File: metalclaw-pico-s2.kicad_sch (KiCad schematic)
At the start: 73 parts, among them J1 USB_C_Receptacle_USB2.0_14P, J2 Conn_01x05, J3 Conn_02x05_Odd_Even, J4 Conn_Coaxial, SW1 SW_Push, SW2 SW_Push, U1 ESP32-S2, U2 MX25L3236FM2I-08G-TR, U3 APS6404L-3SQRx-SN, U5 XC6220B331MR, Y1 XRCGB40M000F1S2FR0

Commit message: Assign more part numbers
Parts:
- C10, C11, C2: footprint (none) -> Capacitor_SMD:C_0402_1005Metric
- C12, C13, C16, C17: footprint Capacitor_SMD:C_0402_1005Metric -> Capacitor_SMD:C_0201_0603Metric
- C14, C15, C4, C7, C8, C9: footprint (none) -> Capacitor_SMD:C_0201_0603Metric
- C5, C6: footprint Capacitor_SMD:C_0402_1005Metric -> Capacitor_SMD:C_0201_0603Metric; Mouser GRT1555C1H6R0DA02D -> 81-GRM0335C1E6R0BA1D
- D1: footprint (none) -> Diode_SMD:D_SOD-323F; Mouser (none) -> 757-CUHS20F30H3F
- L1: footprint Inductor_SMD:L_0402_1005Metric -> Inductor_SMD:L_0201_0603Metric
- R1, R17, R29, R30, R31, R32, R33, R34, R35, R36, R37, R38, R39, R40, R41, R42: footprint Resistor_SMD:R_0402_1005Metric -> Resistor_SMD:R_0201_0603Metric; Mouser (none) -> 71-CRCW02015K10FEDAT
- R10, R11, R12, R13, R14, R15, R16, R18, R19, R2, R20, R21, R22, R23, R24, R25, R26, R27, R28, R3, R4, R5, R6, R7, R8, R9: footprint Resistor_SMD:R_0402_1005Metric -> Resistor_SMD:R_0201_0603Metric; Mouser (none) -> 603-AC0201FR-13220RL
- SW1, SW2: footprint Button_Switch_SMD:SW_Push_SPST_NO_Alps_SKRK -> Button_Switch_SMD:SW_SPST_PTS810; Mouser (none) -> 611-PTS810SJM250SMTR

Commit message: Remove unecessary symbol fields
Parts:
- Y1: private KLC_S4.1 -> (none)
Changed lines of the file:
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@@
-			)
-		)
-		(property private "KLC_S3.3" "The rectangle is not a symbol body but a graphical element"
-			(at 135.89 139.7 0)
-			(show_name yes)
-			(effects
-				(font
-					(size 1.27 1.27)
-				)
-				(hide yes)
-			)
-		)
-		(property private "KLC_S4.1" "Some pins are on 50mil grid to make the symbol small"
-			(at 138.43 139.7 0)
-			(show_name yes)
-			(effects
-				(font
-					(size 1.27 1.27)
-				)
-				(hide yes)
 			)
 		)

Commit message: Specify more passive component parts
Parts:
- C1, C3: Mouser 0603X106M100CT -> 791-0603X106M100CT
- C10, C11, C2: Mouser (none) -> 791-0201X105M100CT
- C14, C15, C16, C17, C4, C7, C8, C9: Mouser (none) -> 81-GRM033R61A104ME5D
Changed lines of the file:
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@@
 			)
 		)
+		(property "Mouser" "81-GRM033R61A104ME5D "
+			(at 40.64 125.73 90)
+			(effects
+				(font
+					(size 1.27 1.27)
+				)
+				(hide yes)
+			)
+		)
 		(pin "1"
 		)
@@
 			)
 		)
+		(property "Mouser" "81-GRM033R61A104ME5D "
+			(at 40.64 138.43 90)
+			(effects
+				(font
+					(size 1.27 1.27)
+				)
+				(hide yes)
+			)
+		)
 		(pin "1"
 		)
@@
 			)
 		)
+		(property "Mouser" "81-GRM033R61A104ME5D "
+			(at 40.64 151.13 90)
+			(effects
+				(font
+					(size 1.27 1.27)
+				)
+				(hide yes)
+			)
+		)
 		(pin "1"
 		)
@@
 			)
 		)
+		(property "Mouser" "81-GRM033R61A104ME5D "
+			(at 40.64 144.78 90)
+			(effects
+				(font
+					(size 1.27 1.27)
+				)
+				(hide yes)
+			)
+		)
 		(pin "1"
 		)
@@
 			)
 		)
-		(property "Mouser" "0603X106M100CT"
+		(property "Mouser" "791-0603X106M100CT "
 			(at 220.98 45.72 0)
 			(effects
@@
 			)
 		)
+		(property "Mouser" "81-GRM033R61A104ME5D "
+			(at 40.64 132.08 90)
+			(effects
+				(font
+					(size 1.27 1.27)
+				)
+				(hide yes)
+			)
+		)
 		(pin "1"
 		)
@@
 			)
 		)
+		(property "Mouser" "81-GRM033R61A104ME5D "
+			(at 193.04 52.07 90)
+			(effects
+				(font
+					(size 1.27 1.27)
+				)
+				(hide yes)
+			)
+		)
 		(pin "1"
 		)
@@
 			)
 		)
-		(property "Mouser" "0603X106M100CT"
+		(property "Mouser" "791-0603X106M100CT "
 			(at 266.7 45.72 0)
 			(effects
@@
 			)
 		)
+		(property "Mouser" "791-0201X105M100CT "
+			(at 40.64 163.83 90)
+			(effects
+				(font
+					(size 1.27 1.27)
+				)
+				(hide yes)
+			)
+		)
 		(pin "1"
 		)
@@
 			)
 		)
+		(property "Mouser" "81-GRM033R61A104ME5D "
+			(at 175.26 52.07 90)
+			(effects
+				(font
+					(size 1.27 1.27)
+				)
+				(hide yes)
+			)
+		)
 		(pin "1"
 		)
@@
 			)
 		)
+		(property "Mouser" "791-0201X105M100CT "
+			(at 40.64 170.18 90)
+			(effects
+				(font
+					(size 1.27 1.27)
+				)
+				(hide yes)
+			)
+		)
 		(pin "1"
 		)
@@
 			)
 		)
+		(property "Mouser" "791-0201X105M100CT "
+			(at 115.57 160.02 90)
+			(effects
+				(font
+					(size 1.27 1.27)
+				)
+				(hide yes)
+			)
+		)
 		(pin "2"
 		)
@@
 			(effects
 				(font
+					(size 1.27 1.27)
+				)
+				(hide yes)
+			)
+		)
+		(property "Mouser" "81-GRM033R61A104ME5D "
+			(at 40.64 157.48 90)
+			(effects
+				(font

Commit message: Some refinements to schematic and layout
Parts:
- C12, C13, J4, L1: now not fitted
- C16, C17: value 100n -> 1u; Mouser 81-GRM033R61A104ME5D -> 791-0201X105M100CT
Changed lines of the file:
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@@
 		(in_bom yes)
 		(on_board yes)
-		(dnp no)
+		(dnp yes)
 		(property "Reference" "C13"
 			(at 132.334 75.692 90)
@@
 		(dnp no)
 		(property "Reference" "C17"
-			(at 188.976 50.292 90)
+			(at 186.182 53.086 0)
 			(effects
 				(font
@@
 			)
 		)
-		(property "Value" "100n"
-			(at 186.69 49.784 90)
+		(property "Value" "1u"
+			(at 187.452 50.8 0)
 			(effects
 				(font
@@
 			)
 		)
-		(property "Mouser" "81-GRM033R61A104ME5D "
+		(property "Mouser" "791-0201X105M100CT "
 			(at 193.04 52.07 90)
 			(effects
@@
 		(in_bom yes)
 		(on_board yes)
-		(dnp no)
+		(dnp yes)
 		(property "Reference" "C12"
 			(at 132.334 86.106 90)
@@
 		(in_bom yes)
 		(on_board yes)
-		(dnp no)
+		(dnp yes)
 		(property "Reference" "J4"
 			(at 147.828 72.136 90)
@@
 		(dnp no)
 		(property "Reference" "C16"
-			(at 171.196 50.292 90)
+			(at 168.402 53.086 0)
 			(effects
 				(font
@@
 			)
 		)
-		(property "Value" "100n"
-			(at 168.91 49.784 90)
+		(property "Value" "1u"
+			(at 169.672 50.546 0)
 			(effects
 				(font
@@
 			)
 		)
-		(property "Mouser" "81-GRM033R61A104ME5D "
+		(property "Mouser" "791-0201X105M100CT "
 			(at 175.26 52.07 90)
 			(effects
@@
 		(in_bom yes)
 		(on_board yes)
-		(dnp no)
+		(dnp yes)
 		(property "Reference" "L1"
 			(at 114.808 77.47 0)

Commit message: Fix all ERC errors and warnings
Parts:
- removed D1: D_Schottky, Diode_SMD:D_SOD-323F, symbol Device:D_Schottky
- added JP1: Jumper_2_Bridged, symbol Jumper:Jumper_2_Bridged
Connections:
- net +3V3: no longer A2.36 (3V3), U1.30 (VDD_SPI)
- net GND: now also JP1.2 (B); no longer A2.33 (AGND)
- net GP14: no longer R27.2, R31.2, R40.2, U1.55 (GPIO46)
- net GP6: no longer R17.2, R19.2, U1.21 (XTAL_32K_P)
- net VBUS: now also C1.1, U5.1 (VIN), U5.3 (CE)
- net +3.3V renamed VDD
- net VDD: now also U1.30 (VDD_SPI)
- removed net VS: A2.39 (VSYS), C1.1, U5.1 (VIN), U5.3 (CE)
- new net: A2.33 (AGND), JP1.1 (A)
- new net GP15: R27.2, R31.2, R40.2, U1.55 (GPIO46)
- new net GP7: R17.2, R19.2, U1.21 (XTAL_32K_P)
- no-connect marks 2 -> 4

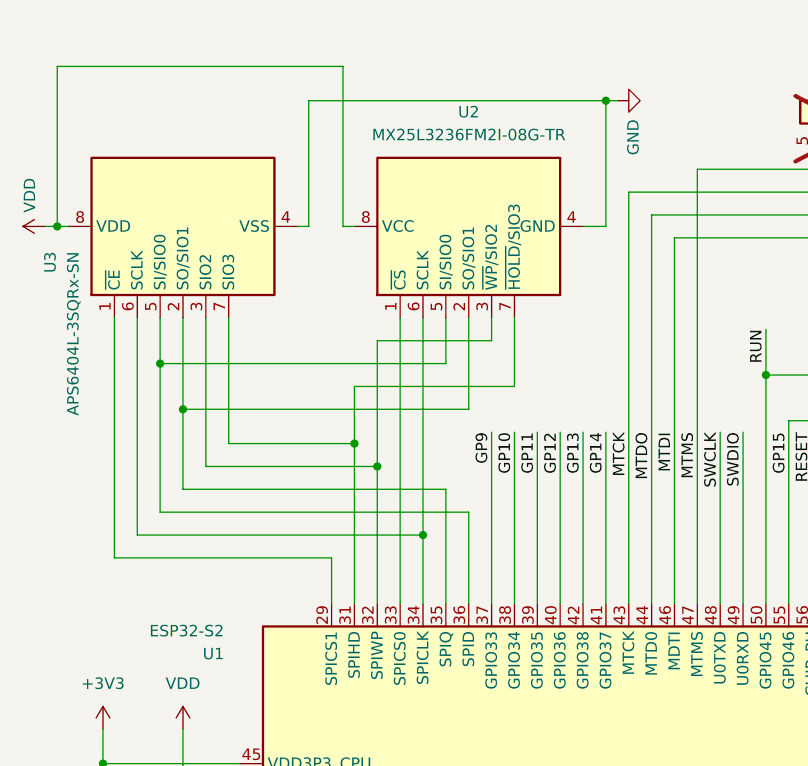
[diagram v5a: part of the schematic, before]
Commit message: Add bypass caps to PSRAM and flash
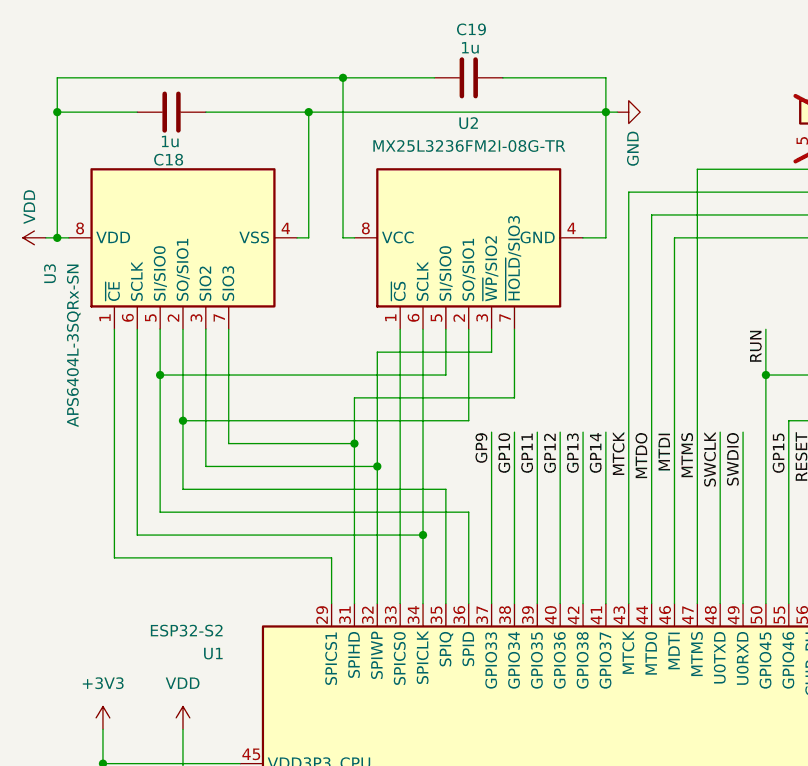
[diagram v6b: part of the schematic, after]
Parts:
- added C18, C19: 1u, Capacitor_SMD:C_0402_1005Metric, symbol Device:C
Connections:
- net GND: now also C18.1, C19.2
- net VDD: now also C18.2, C19.1
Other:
- moved on the sheet: U2, U3

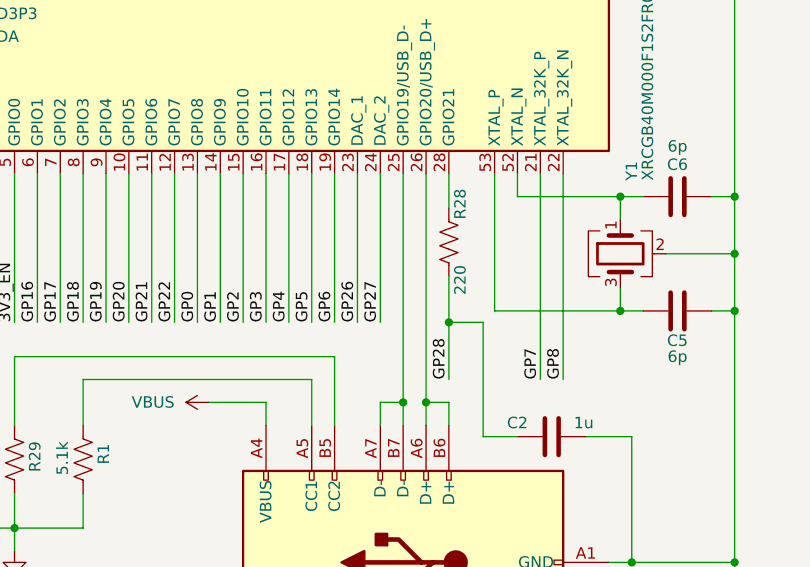
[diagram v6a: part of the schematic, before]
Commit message: Initial routing left side resistors
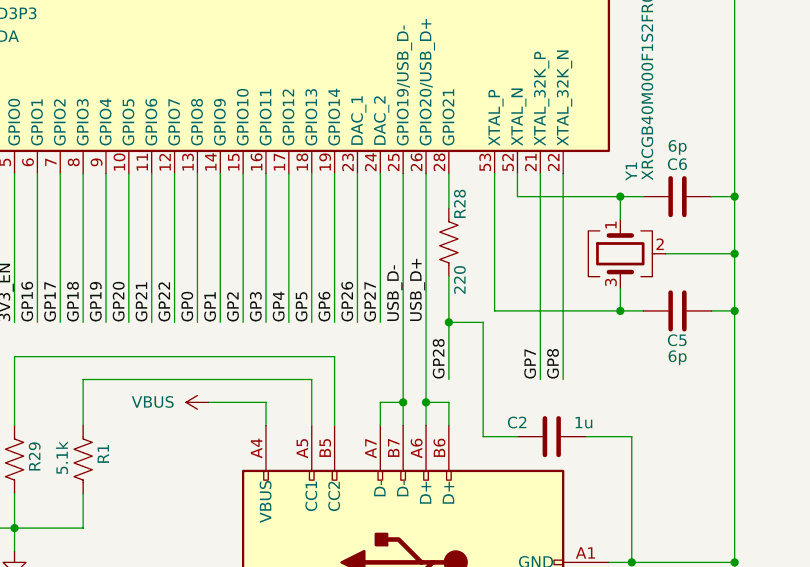
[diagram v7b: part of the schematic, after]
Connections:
- net USB_D+: now reaches J1.A6 (D+), J1.B6 (D+), U1.26 (GPIO20/USB_D+)
- net USB_D-: now reaches J1.A7 (D-), J1.B7 (D-), U1.25 (GPIO19/USB_D-)
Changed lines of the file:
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@@
+		)
+	)
+	(label "USB_D-"
+		(at 99.06 147.32 90)
+		(effects
+			(font
+				(size 1.27 1.27)
+			)
+			(justify left bottom)
 		)
 	)
@@
 		(effects
 			(font
+				(size 1.27 1.27)
+			)
+			(justify left bottom)
+		)
+	)
+	(label "USB_D+"
+		(at 101.6 147.32 90)
+		(effects
+			(font

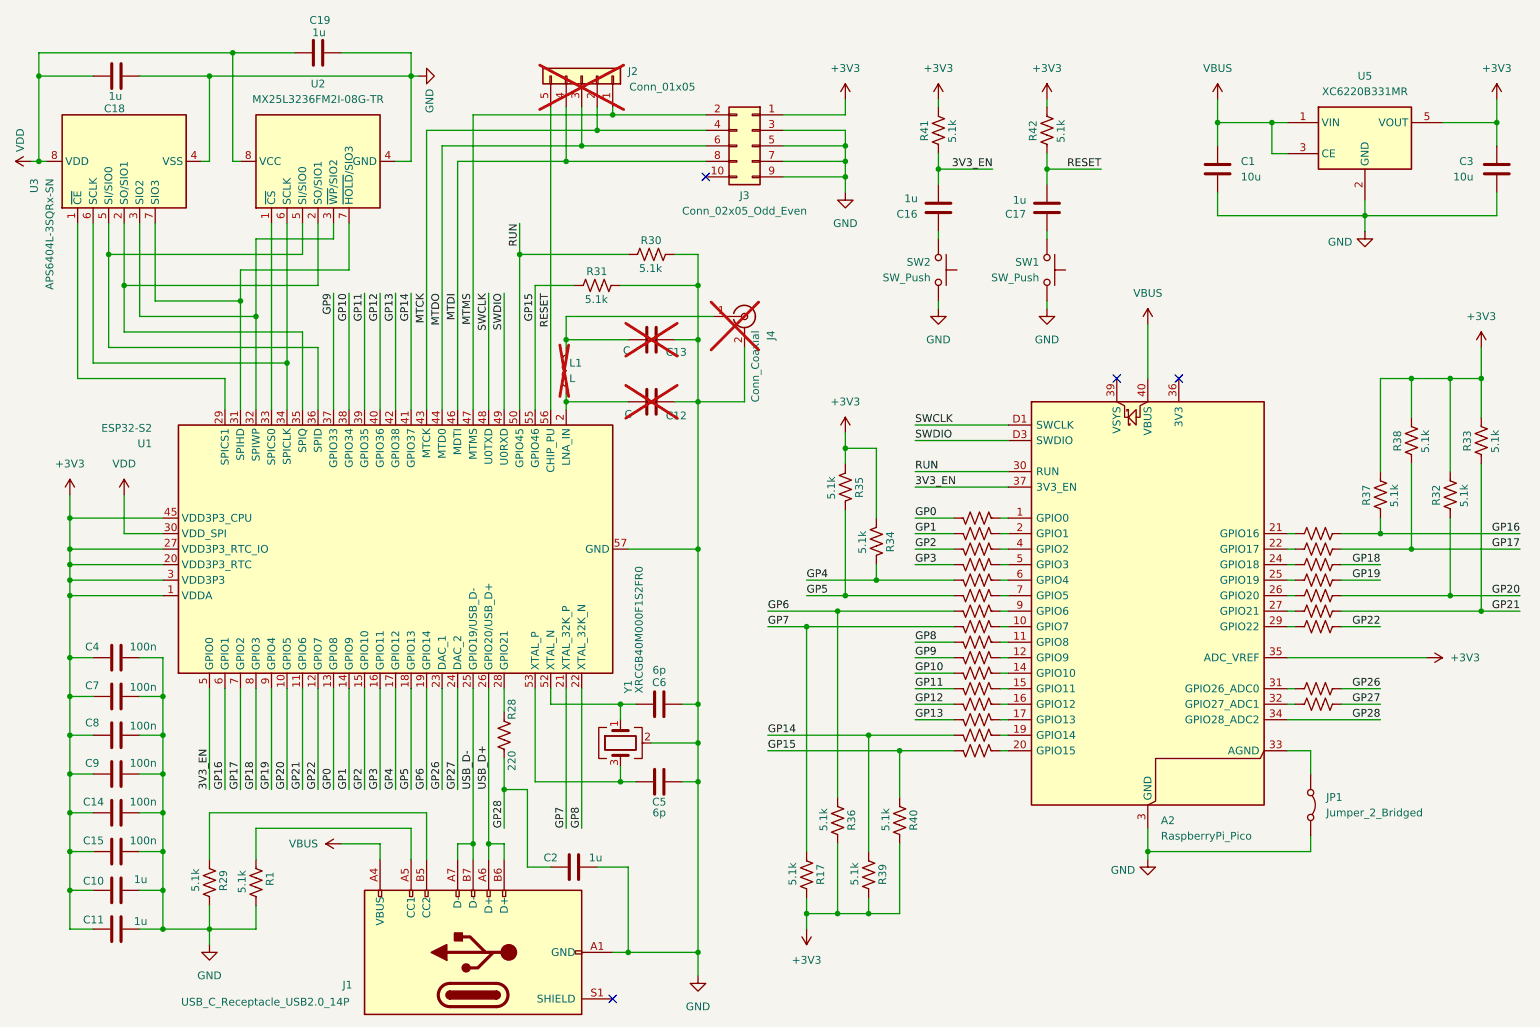
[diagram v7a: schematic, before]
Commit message: Change I2C pins
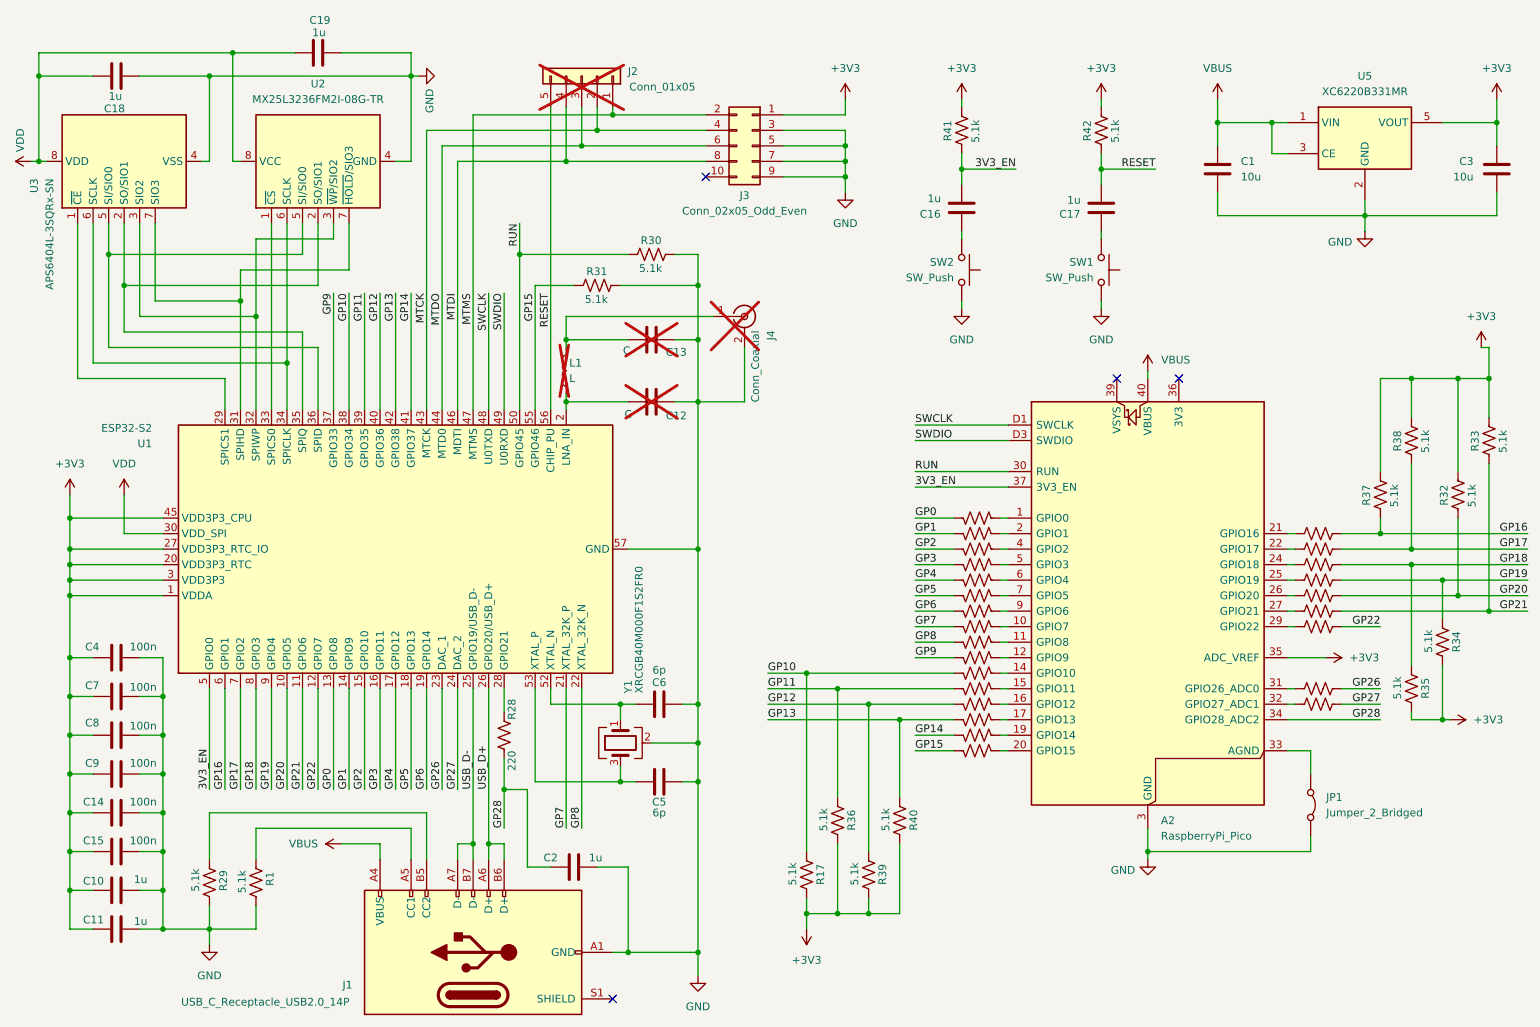
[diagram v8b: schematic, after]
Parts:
- C10, C11, C18, C19, C2: footprint Capacitor_SMD:C_0402_1005Metric -> Capacitor_SMD:C_0201_0603Metric
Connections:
- net GP10: now also R17.2
- net GP11: now also R36.2
- net GP12: now also R39.2
- net GP13: now also R40.2
- net GP14: no longer R39.2
- net GP15: no longer R40.2
- net GP18: now also R35.2
- net GP19: now also R34.2
- net GP4: no longer R34.2
- net GP5: no longer R35.2
- net GP6: no longer R36.2
- net GP7: no longer R17.2
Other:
- moved on the sheet: C16, C17, R32, R33, R34, R35, R41, R42, SW1, SW2
